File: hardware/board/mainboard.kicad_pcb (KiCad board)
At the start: 4 copper layers, 60 x 110 mm, 266 parts, among them J201 Power, Q601 BCM847, Q701 BCM847, Q801 BCM847, U1 TL074, U2 TL074, U201 TL431A, U3 TL074, U4 TL074, U5 TL074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

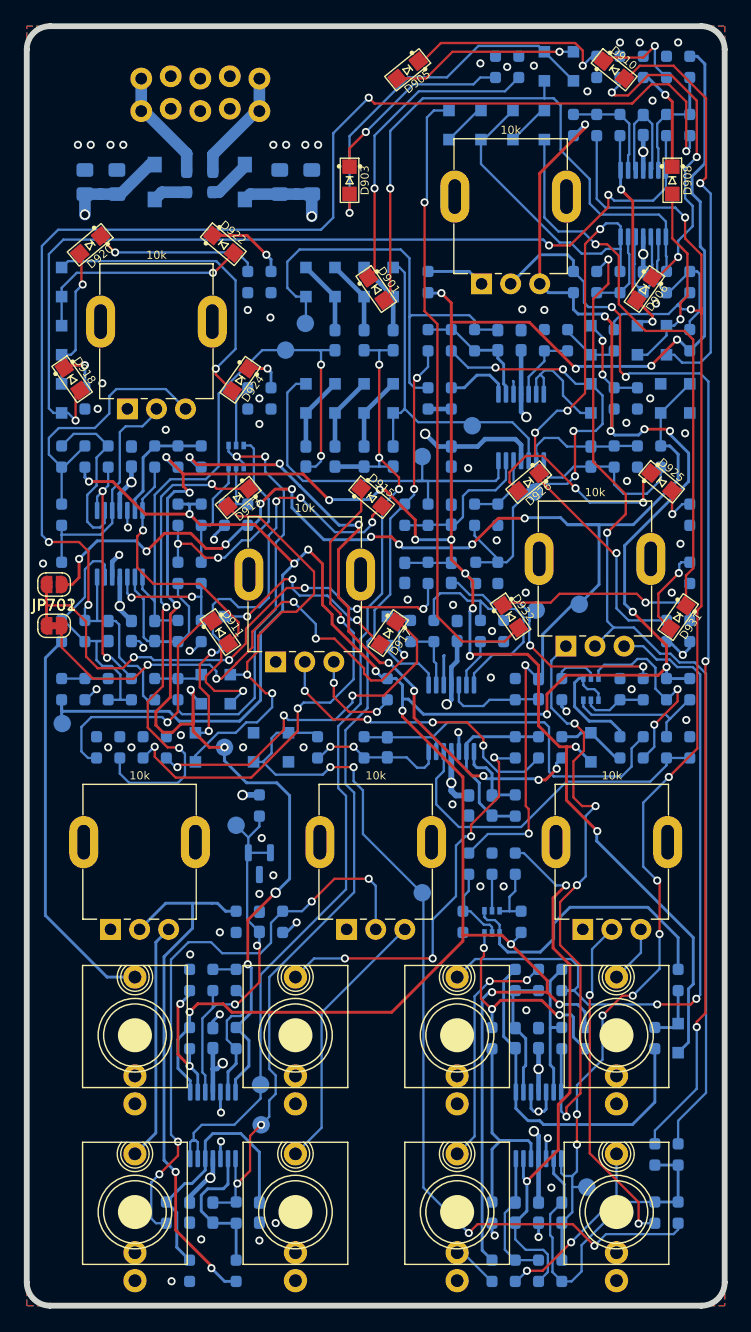
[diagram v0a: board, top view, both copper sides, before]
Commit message: hardware: reduce size of power traces, give vias a little more clearance
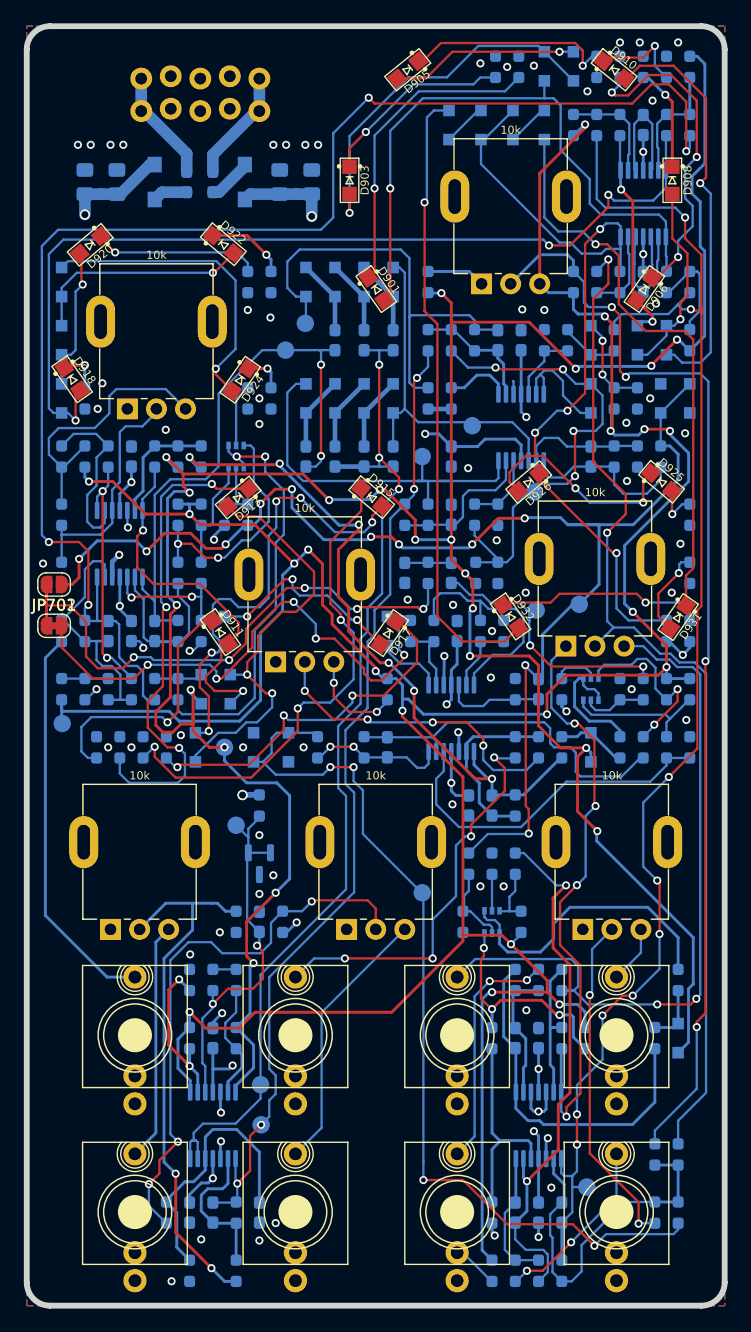
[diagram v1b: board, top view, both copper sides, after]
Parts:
- turned R718 to 90 degrees
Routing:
- net Net-(R304-Pad1): track 51.2 -> 48.2 mm, vias 4 -> 3
- net Net-(U1C--): track 11.0 -> 13.9 mm
- net Net-(U5B--): track 32.3 -> 30.1 mm
- net /Instability VCA/INSTABILITY_CV_OUT: track 61.7 -> 59.6 mm, vias 8 -> 6
- net Net-(Q701-C-Pad6): track 17.9 -> 16.0 mm
- net Net-(R404-Pad1): track 52.9 -> 51.6 mm
- net /Cutoff CV Driver/INSTABILITY_IN: track 79.8 -> 78.8 mm
- net -8VREF: track 239.4 -> 240.1 mm
- net Net-(U1B-+): track 22.7 -> 23.3 mm
- net +8VREF: track 275.3 -> 275.9 mm
- net GND: track 53.8 -> 54.0 mm, vias 78 -> 79

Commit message: Added stitching vias and cleaned various things up.
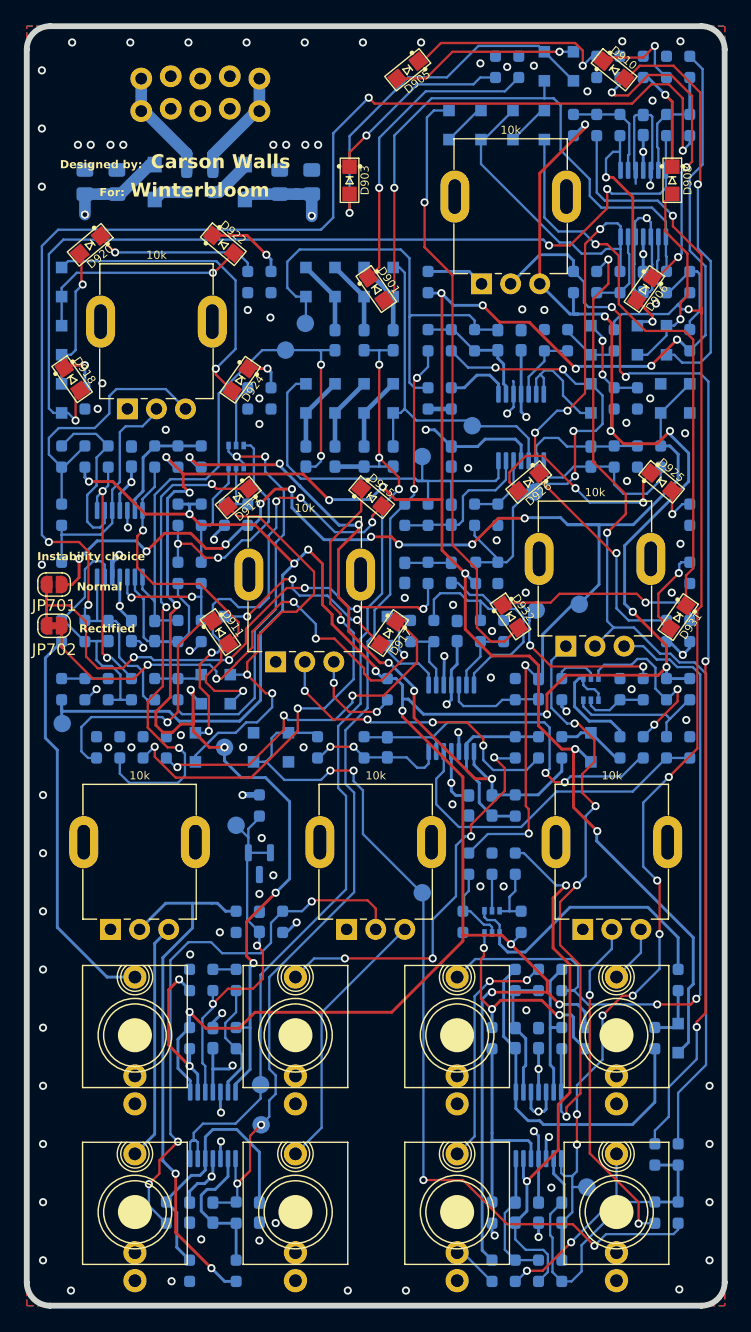
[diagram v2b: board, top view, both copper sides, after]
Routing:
- net GND: track 54.0 -> 64.1 mm, vias 79 -> 108
- net -8VREF: track 240.1 -> 236.3 mm, vias 20 -> 17
- net Net-(D906-A): track 17.6 -> 20.9 mm
- net +12V: track 263.5 -> 261.1 mm
- net +8VREF: track 275.9 -> 277.8 mm, vias 18 -> 17
- net Net-(U5B--): track 30.1 -> 31.6 mm, vias 0 -> 2
- net Net-(D930-K): track 53.9 -> 52.5 mm
- net Net-(R404-Pad1): track 51.6 -> 52.5 mm
- net Net-(D906-K): track 27.8 -> 26.9 mm
- net /Cutoff CV Driver/CUTOFF_OUT: track 125.0 -> 124.2 mm
- net Net-(D901-A): track 53.3 -> 52.5 mm
- net Net-(Q801-E-Pad1): track 25.6 -> 24.8 mm
- net Net-(U2B-+): track 18.6 -> 17.9 mm
- net /Instability VCA/INSTABILITY_CV_OUT: track 59.6 -> 60.3 mm
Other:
- board text added: "Carson Walls"
- board text added: "Designed by:"
- board text added: "For:"
- board text added: "Instability choice"
- board text added: "Normal"
- board text added: "Rectified"
- board text added: "Winterbloom"
